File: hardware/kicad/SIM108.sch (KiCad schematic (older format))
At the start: 39 parts, among them J1 Screw_Terminal_01x09, J2 CAN, SW1 PRG, SW2 INSTANCE, SW3 BUS, U1 MCP2551-I-P, U2 TMR_2411, U3 MAX6816, U4 74HC595, U5 Teensy_3.2

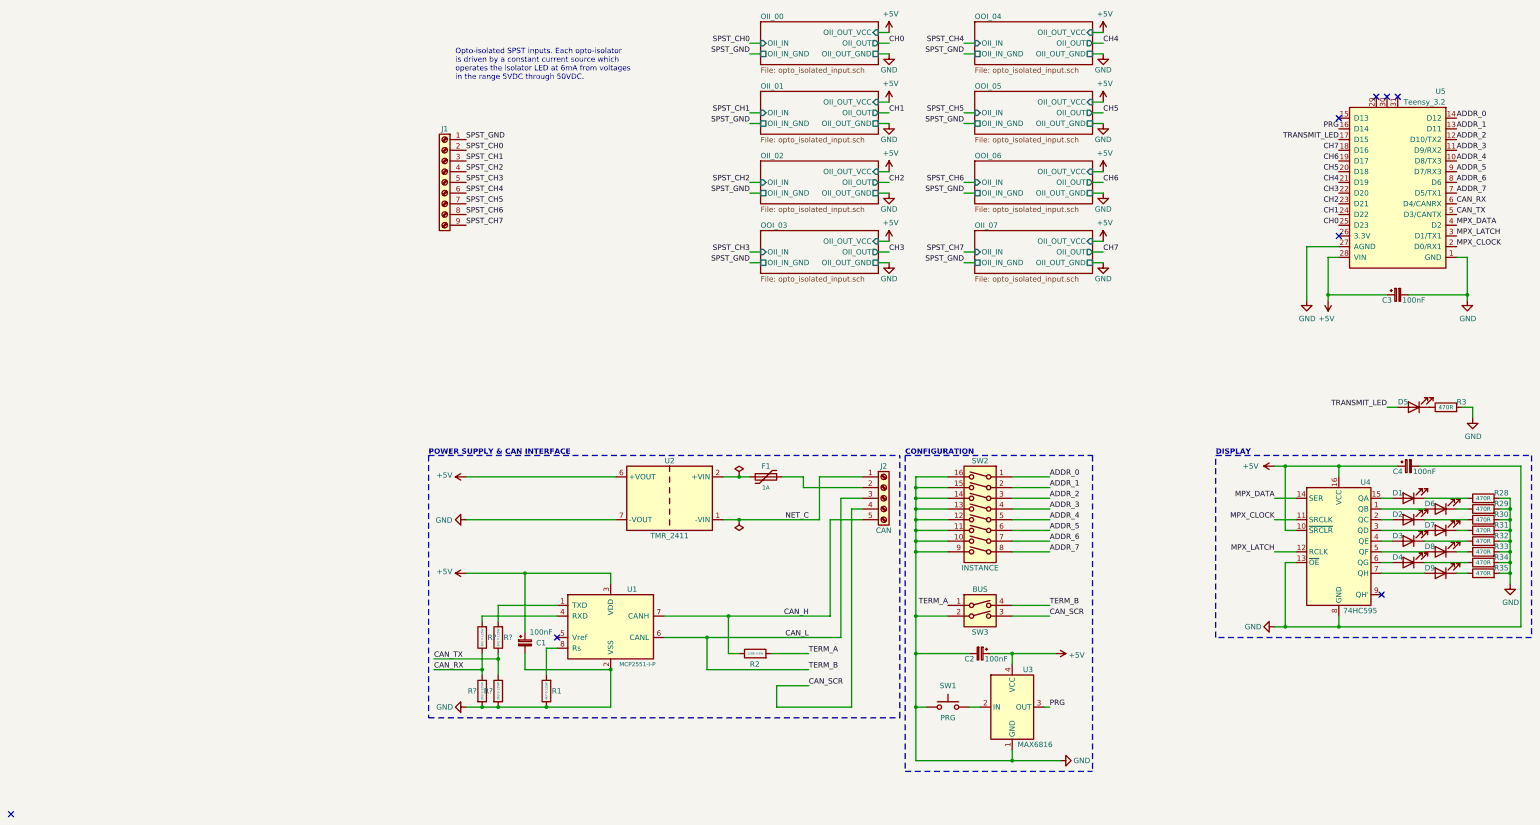
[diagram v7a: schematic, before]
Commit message: Migrate to Teens 4.0
3.3V inputs
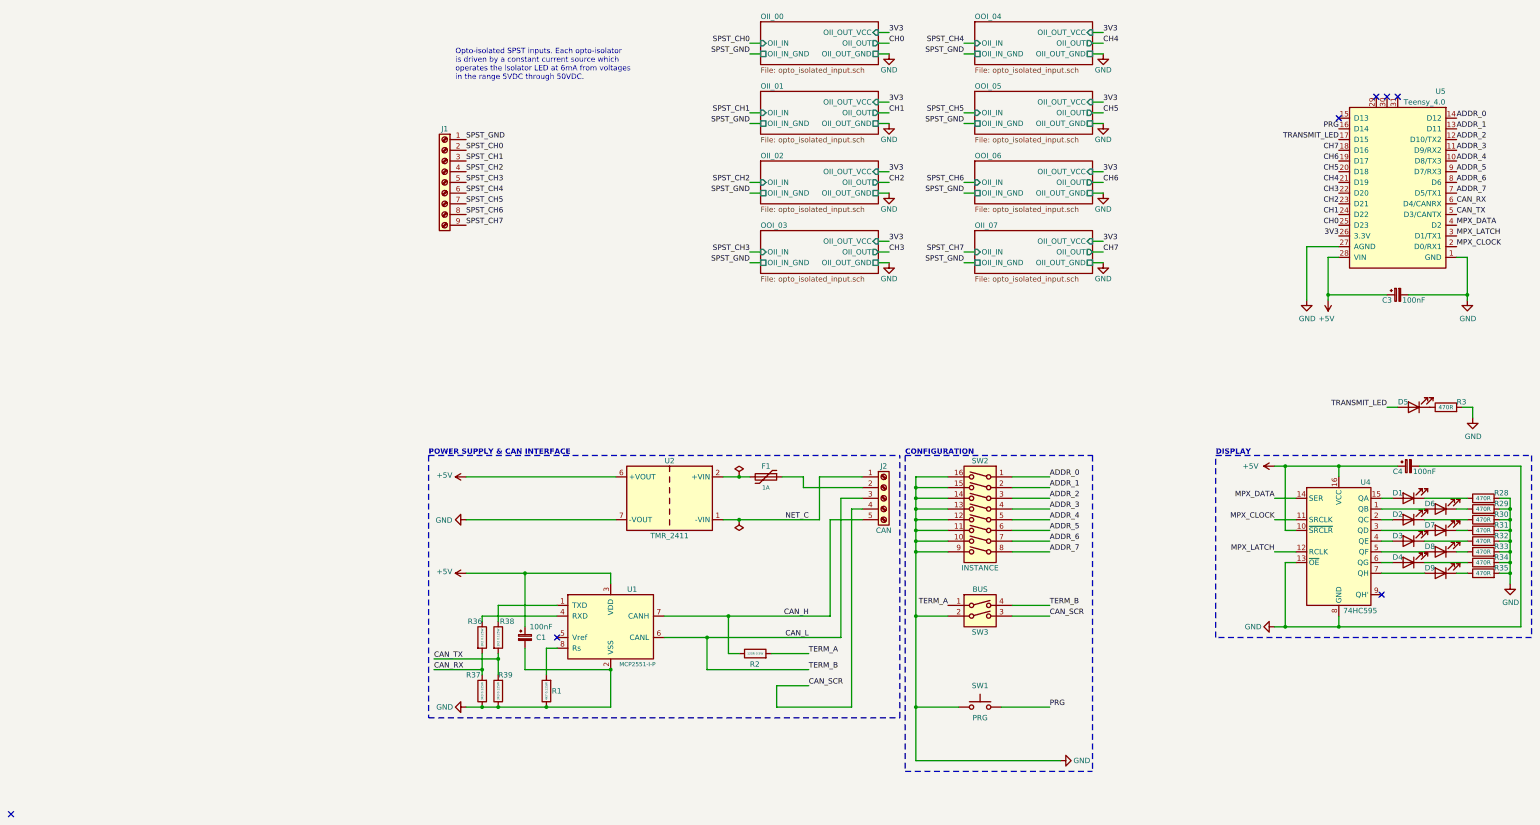
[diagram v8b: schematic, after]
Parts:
- removed C2: 100nF, Capacitor_THT:CP_Radial_D5.0mm_P2.00mm, symbol Device:CP_Small
- removed U3: MAX6816, Package_TO_SOT_SMD:SOT-143, symbol Interface:MAX6816
- U5: value Teensy_3.2 -> Teensy_4.0
- gave numbers to parts that had none: 4
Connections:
- net CAN_RX: now also R36.2, R37.2; no longer R36.1, R37.1
- net CAN_TX: now also R38.2, R39.2; no longer R38.1, R39.1
- net GND: now also R37.1, R39.1; no longer R37.2, R39.2
- net PRG: now also SW1.2
- net at U1.1 (TXD): now also R38.1; no longer R38.2
- net at U1.4 (RXD): now also R36.1; no longer R36.2
- net 3V3: now reaches U5.26 (3.3V)
- no-connect marks 8 -> 7
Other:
- moved on the sheet: C1, SW1
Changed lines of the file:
@@
 Wire Wire Line
 	10350 2900 10250 2900
-NoConn ~ 9150 2700
 Text Label 10250 2400 0    50   ~ 0
 CAN_RX
@@
 P 10250 2900
 F 0 "U5" H 10400 1350 50  0000 C CNN
-F 1 "Teensy_3.2" H 10550 1450 50  0000 C CNN
+F 1 "Teensy_4.0" H 10550 1450 50  0000 C CNN
 F 2 "Package_DIP:DIP-28_W15.24mm_LongPads" H 10250 2900 50  0001 C CNN
 F 3 "" H 10250 2900 50  0001 C CNN
@@
 Wire Wire Line
 	1000 5850 1550 5850
-Wire Wire Line
-	1000 7100 1150 7100
 Text Label 700  6750 0    50   ~ 0
 CAN_RX
@@
 	3400 5350 3550 5350
 Wire Wire Line
-	1550 6400 1550 5850
-Wire Wire Line
-	1550 6750 1550 6600
+	1550 6350 1550 5850
+Wire Wire Line
+	1550 6750 1550 6550
 $Comp
 L power:PWR_FLAG #FLG01
@@
 L Switch:SW_Push SW1
 U 1 1 633332C8
-P 5500 7100
-F 0 "SW1" H 5500 7300 50  0000 C CNN
-F 1 "PRG" H 5500 7000 50  0000 C CNN
-F 2 "PDJR_Switches:PCB_PUSH_BUTTON_10mm" H 5500 7300 50  0001 C CNN
-F 3 "~" H 5500 7300 50  0001 C CNN
-	1    5500 7100
-	1    0    0    -1
-$EndComp
-Wire Wire Line
-	5200 6250 5200 6600
+P 5800 7100
+F 0 "SW1" H 5800 7300 50  0000 C CNN
+F 1 "PRG" H 5800 7000 50  0000 C CNN
+F 2 "PDJR_Switches:PCB_PUSH_BUTTON_10mm" H 5800 7300 50  0001 C CNN
+F 3 "~" H 5800 7300 50  0001 C CNN
+	1    5800 7100
+	1    0    0    -1
+$EndComp
 Text Label 6450 7100 0    50   ~ 0
 PRG
@@
 L Device:CP_Small C1
 U 1 1 635FBF50
-P 1550 6500
-F 0 "C1" H 1700 6500 50  0000 C CNN
-F 1 "100nF" H 1700 6600 50  0000 C CNN
-F 2 "Capacitor_THT:CP_Radial_D5.0mm_P2.00mm" H 1550 6500 50  0001 C CNN
-F 3 "~" H 1550 6500 50  0001 C CNN
-	1    1550 6500
+P 1550 6450
+F 0 "C1" H 1700 6450 50  0000 C CNN
+F 1 "100nF" H 1700 6550 50  0000 C CNN
+F 2 "Capacitor_THT:CP_Radial_D5.0mm_P2.00mm" H 1550 6450 50  0001 C CNN
+F 3 "~" H 1550 6450 50  0001 C CNN
+	1    1550 6450
 	1    0    0    -1
 $EndComp
@@
 Wire Wire Line
 	5500 5650 5200 5650
-$Comp
-L Interface:MAX6816 U3
-U 1 1 6336163A
-P 6100 7100
-F 0 "U3" H 6200 7450 50  0000 L CNN
-F 1 "MAX6816" H 6150 6750 50  0000 L CNN
-F 2 "Package_TO_SOT_SMD:SOT-143" H 6750 6650 50  0001 C CNN
-F 3 "https://datasheets.maximintegrated.com/en/ds/1896.pdf" H 6100 7100 50  0001 C CNN
-	1    6100 7100
-	1    0    0    -1
-$EndComp
-Wire Wire Line
-	6100 7500 6100 7600
-Wire Wire Line
-	5800 7100 5700 7100
-Wire Wire Line
-	6100 6700 6100 6600
-Wire Wire Line
-	6100 6600 6500 6600
-$Comp
-L Device:CP_Small C2
-U 1 1 6355CB0C
-P 5800 6600
-F 0 "C2" V 5850 6500 50  0000 C CNN
-F 1 "100nF" V 5850 6750 50  0000 C CNN
-F 2 "Capacitor_THT:CP_Radial_D5.0mm_P2.00mm" H 5800 6600 50  0001 C CNN
-F 3 "~" H 5800 6600 50  0001 C CNN
-	1    5800 6600
-	0    1    1    0
-$EndComp
-Wire Wire Line
-	5700 6600 5200 6600
-Connection ~ 5200 6600
 Connection ~ 5200 6250
 Wire Wire Line
-	5900 6600 6100 6600
-Connection ~ 6100 6600
-Wire Wire Line
-	6400 7100 6450 7100
-Wire Wire Line
-	6100 7600 5200 7600
-Wire Wire Line
-	5200 6600 5200 7100
-Wire Wire Line
-	5300 7100 5200 7100
+	5600 7100 5200 7100
 Connection ~ 5200 7100
 Wire Wire Line
 	5200 7100 5200 7600
-$Comp
-L power:+5V #PWR013
-U 1 1 6369DCBF
-P 6500 6600
-F 0 "#PWR013" H 6500 6450 50  0001 C CNN
-F 1 "+5V" V 6515 6728 50  0000 L CNN
-F 2 "" H 6500 6600 50  0001 C CNN
-F 3 "" H 6500 6600 50  0001 C CNN
-	1    6500 6600
-	0    1    1    0
-$EndComp
 $Comp
 L power:GND #PWR014
@@
 $EndComp
 Wire Wire Line
-	6550 7600 6100 7600
-Connection ~ 6100 7600
-Wire Wire Line
 	6100 4950 6450 4950
 Wire Wire Line
@@
 Wire Wire Line
 	4850 900  4950 900
-$Comp
-L power:+5V #PWR05
-U 1 1 634AE8DC
-P 4950 800
-F 0 "#PWR05" H 4950 650 50  0001 C CNN
-F 1 "+5V" H 4965 973 50  0000 C CNN
-F 2 "" H 4950 800 50  0001 C CNN
-F 3 "" H 4950 800 50  0001 C CNN
-	1    4950 800
-	1    0    0    -1
-$EndComp
 $Sheet
 S 3750 1350 1100 400
@@
 F6 "OII_OUT_VCC" I R 4850 1450 50
 $EndSheet
-$Comp
-L power:+5V #PWR07
-U 1 1 63462A09
-P 4950 1450
-F 0 "#PWR07" H 4950 1300 50  0001 C CNN
-F 1 "+5V" H 4965 1623 50  0000 C CNN
-F 2 "" H 4950 1450 50  0001 C CNN
-F 3 "" H 4950 1450 50  0001 C CNN
-	1    4950 1450
-	1    0    0    -1
-$EndComp
 Wire Wire Line
 	3650 1550 3750 1550
@@
 Wire Wire Line
 	4850 1650 4950 1650
-$Comp
-L power:+5V #PWR09
-U 1 1 634E105F
-P 4950 2100
-F 0 "#PWR09" H 4950 1950 50  0001 C CNN
-F 1 "+5V" H 4965 2273 50  0000 C CNN
-F 2 "" H 4950 2100 50  0001 C CNN
-F 3 "" H 4950 2100 50  0001 C CNN
-	1    4950 2100
-	1    0    0    -1
-$EndComp
 Wire Wire Line
 	4850 2100 4950 2100
@@
 Wire Wire Line
 	4850 2950 4950 2950
-$Comp
-L power:+5V #PWR011
-U 1 1 6351340F
-P 4950 2750
-F 0 "#PWR011" H 4950 2600 50  0001 C CNN
-F 1 "+5V" H 4965 2923 50  0000 C CNN
-F 2 "" H 4950 2750 50  0001 C CNN
-F 3 "" H 4950 2750 50  0001 C CNN
-	1    4950 2750
-	1    0    0    -1
-$EndComp
 Wire Wire Line
 	3650 2950 3750 2950
 Wire Wire Line
 	6850 1000 6950 1000
-$Comp
-L power:+5V #PWR015
-U 1 1 6352F708
-P 6950 800
-F 0 "#PWR015" H 6950 650 50  0001 C CNN
-F 1 "+5V" H 6965 973 50  0000 C CNN
-F 2 "" H 6950 800 50  0001 C CNN
-F 3 "" H 6950 800 50  0001 C CNN
-	1    6950 800
-	1    0    0    -1
-$EndComp
 Wire Wire Line
 	5750 1000 5650 1000
@@
 Wire Wire Line
 	6850 2950 6950 2950
-$Comp
-L power:+5V #PWR017
-U 1 1 6359AF9F
-P 6950 1450
-F 0 "#PWR017" H 6950 1300 50  0001 C CNN
-F 1 "+5V" H 6965 1623 50  0000 C CNN
-F 2 "" H 6950 1450 50  0001 C CNN
-F 3 "" H 6950 1450 50  0001 C CNN
-	1    6950 1450
-	1    0    0    -1
-$EndComp
-$Comp
-L power:+5V #PWR019
-U 1 1 6359B793
-P 6950 2100
-F 0 "#PWR019" H 6950 1950 50  0001 C CNN
-F 1 "+5V" H 6965 2273 50  0000 C CNN
-F 2 "" H 6950 2100 50  0001 C CNN
-F 3 "" H 6950 2100 50  0001 C CNN
-	1    6950 2100
-	1    0    0    -1
-$EndComp
-$Comp
-L power:+5V #PWR021
-U 1 1 6359BE30
-P 6950 2750
-F 0 "#PWR021" H 6950 2600 50  0001 C CNN
-F 1 "+5V" H 6965 2923 50  0000 C CNN
-F 2 "" H 6950 2750 50  0001 C CNN
-F 3 "" H 6950 2750 50  0001 C CNN
-	1    6950 2750
-	1    0    0    -1
-$EndComp
 Text Label 5650 2950 2    50   ~ 0
 SPST_GND
@@
 	10750 5750 10750 5850
 $Comp
-L Device:R R?
+L Device:R R38
 U 1 1 638A66B7
 P 1300 6450
-F 0 "R?" H 1250 6450 50  0000 R CNN
+F 0 "R38" H 1450 6600 50  0000 R CNN
 F 1 "2K2 0.125W" V 1300 6450 20  0000 C CNN
 F 2 "Resistor_THT:R_Axial_DIN0207_L6.3mm_D2.5mm_P2.54mm_Vertical" V 1230 6450 50  0001 C CNN
 F 3 "~" H 1300 6450 50  0001 C CNN
 	1    1300 6450
-	-1   0    0    1
-$EndComp
-$Comp
-L Device:R R?
+	1    0    0    -1
+$EndComp
+$Comp
+L Device:R R39
 U 1 1 638A701E
 P 1300 6950
-F 0 "R?" H 1250 6950 50  0000 R CNN
+F 0 "R39" H 1300 6800 50  0000 R CNN
 F 1 "3K3 0.125W" V 1300 6950 20  0000 C CNN
 F 2 "Resistor_THT:R_Axial_DIN0207_L6.3mm_D2.5mm_P2.54mm_Vertical" V 1230 6950 50  0001 C CNN
 F 3 "~" H 1300 6950 50  0001 C CNN
 	1    1300 6950
-	1    0    0    -1
-$EndComp
-Connection ~ 1300 7100
-Wire Wire Line
-	1300 7100 1750 7100
+	-1   0    0    1
+$EndComp
 Wire Wire Line
 	1300 6300 1300 6150
@@
 	1300 6650 1300 6800
 $Comp
-L Device:R R?
+L Device:R R36
 U 1 1 638DB685
 P 1150 6450
-F 0 "R?" H 1100 6450 50  0000 R CNN
+F 0 "R36" H 1150 6600 50  0000 R CNN
 F 1 "2K2 0.125W" V 1150 6450 20  0000 C CNN
 F 2 "Resistor_THT:R_Axial_DIN0207_L6.3mm_D2.5mm_P2.54mm_Vertical" V 1080 6450 50  0001 C CNN
 F 3 "~" H 1150 6450 50  0001 C CNN
 	1    1150 6450
-	-1   0    0    1
-$EndComp
-$Comp
-L Device:R R?
+	1    0    0    -1
+$EndComp
+$Comp
+L Device:R R37
 U 1 1 638DBDD6
 P 1150 6950
-F 0 "R?" H 1100 6950 50  0000 R CNN
+F 0 "R37" H 1300 6800 50  0000 R CNN
 F 1 "3K3 0.125W" V 1150 6950 20  0000 C CNN
 F 2 "Resistor_THT:R_Axial_DIN0207_L6.3mm_D2.5mm_P2.54mm_Vertical" V 1080 6950 50  0001 C CNN
 F 3 "~" H 1150 6950 50  0001 C CNN
 	1    1150 6950
-	1    0    0    -1
-$EndComp
-Connection ~ 1150 7100
-Wire Wire Line
-	1150 7100 1300 7100
+	-1   0    0    1
+$EndComp
 Wire Wire Line
 	1150 6600 1150 6750
@@
 Wire Wire Line
 	1150 6250 1850 6250
+Wire Wire Line
+	5200 6250 5200 7100
+Wire Wire Line
+	6000 7100 6450 7100
+Wire Wire Line
+	5200 7600 6550 7600
+Connection ~ 1300 7100
+Wire Wire Line
+	1300 7100 1750 7100
+Wire Wire Line
+	1000 7100 1150 7100
+Connection ~ 1150 7100
+Wire Wire Line
+	1150 7100 1300 7100
+Text Label 9150 2700 2    50   ~ 0
+3V3
+Text Label 6950 800  0    50   ~ 0
+3V3
+Text Label 6950 1450 0    50   ~ 0
+3V3
+Text Label 6950 2100 0    50   ~ 0
+3V3
+Text Label 6950 2750 0    50   ~ 0
+3V3
+Text Label 4950 2750 0    50   ~ 0
+3V3
+Text Label 4950 2100 0    50   ~ 0
+3V3
+Text Label 4950 1450 0    50   ~ 0
+3V3
+Text Label 4950 800  0    50   ~ 0
+3V3
 $EndSCHEMATC
